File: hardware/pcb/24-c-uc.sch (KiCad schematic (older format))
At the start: 29 parts, among them J201 ST-LINK, J202 Debug UART, U201 STM32F103C8Tx, Y201 NX3225GD 8MHz

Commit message: First placement
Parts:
- removed TP211: HW-Version, TestPoint:TestPoint_Pad_D2.0mm, symbol Connector:TestPoint
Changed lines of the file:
@@
 Wire Wire Line
 	1400 6250 1400 6200
-Text Label 2000 6600 2    50   ~ 0
+Text Label 2100 6600 2    50   ~ 0
 HW-Version
 Wire Wire Line
@@
 Wire Wire Line
 	8350 4900 8350 4800
-$Comp
-L Connector:TestPoint TP211
-U 1 1 5FF8AEC1
-P 2100 6500
-F 0 "TP211" H 2158 6572 50  0000 L CNN
-F 1 "HW-Version" H 2158 6527 50  0001 L CNN
-F 2 "TestPoint:TestPoint_Pad_D2.0mm" H 2300 6500 50  0001 C CNN
-F 3 "~" H 2300 6500 50  0001 C CNN
-	1    2100 6500
-	1    0    0    -1
-$EndComp
-Wire Wire Line
-	2100 6500 2100 6600
 Wire Wire Line
 	1400 6600 2100 6600

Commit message: Added routing
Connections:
- net RTC-CLK: now reaches U201.25 (PB12)
- no-connect marks 16 -> 15
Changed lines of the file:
@@
 NoConn ~ 6300 3800
 NoConn ~ 6300 4100
-NoConn ~ 5000 4200
 NoConn ~ 5000 3900
 NoConn ~ 5000 3500
@@
 Wire Wire Line
 	3600 2150 3600 2550
+Text HLabel 2400 3850 0    50   Input ~ 0
+RTC-CLK
+Wire Wire Line
+	2400 3850 3000 3850
+Text Label 3000 3850 2    50   ~ 0
+RTC-CLK
+Wire Wire Line
+	4400 4200 5000 4200
+Text Label 4400 4200 0    50   ~ 0
+RTC-CLK
 $EndSCHEMATC

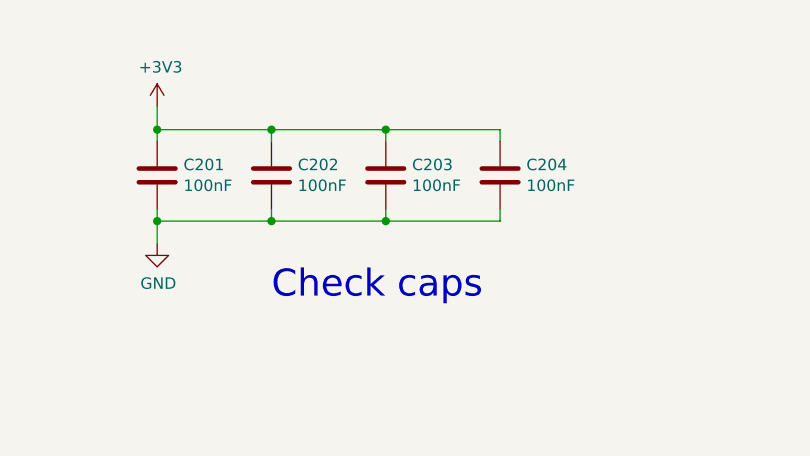
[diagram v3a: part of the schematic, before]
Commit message: Added caps to hall sensors
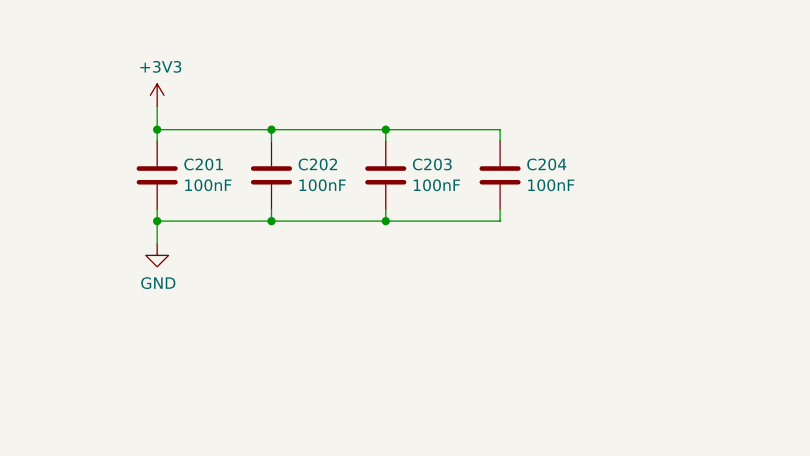
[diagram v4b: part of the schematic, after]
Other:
- note removed: "Check caps"
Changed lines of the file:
@@
 Text Label 9100 4700 0    50   ~ 0
 uC-Debug-Tx
-Text Notes 4800 6900 0    118  ~ 0
-Check caps
 $Comp
 L Connector_Generic:Conn_01x06 J202
